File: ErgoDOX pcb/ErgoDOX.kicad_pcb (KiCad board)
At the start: 2 copper layers, 182.8 x 158.9 mm, 77 parts, among them J1 USB, J2 3.5mm, J3 JMP, J4 JMP, SW0:10 SW0:3, SW0:11 SW0:2, SW0:12 SW0:1, SW0:7 SW0:6, SW0:8 SW0:5, SW0:9 SW0:4, SW1:10 SW1:3, SW1:11 SW1:2, SW1:12 SW1:1, SW1:13 SW1:0, SW1:9 SW1:4, SW2:10 SW2:3, SW2:11 SW2:2, SW2:12 SW2:1, SW2:13 SW2:0, SW2:7 SW2:6, SW2:8 SW2:5, SW2:9 SW2:4, SW3:10 SW3:3, SW3:11 SW3:2, SW3:12 SW3:1, SW3:13 SW3:0, SW3:8 SW3:5, SW3:9 SW3:4, SW4:10 SW4:3, SW4:11 SW4:2, SW4:12 SW4:1, SW4:13 SW4:0, SW4:7 SW4:6, SW4:8 SW4:5, SW4:9 SW4:4, SW5:10 SW5:3, SW5:11 SW5:2, SW5:12 SW5:1, SW5:13 SW5:0, SW5:7 SW5:6, SW5:8 SW5:5, SW5:9 SW5:4, U1 TEENSY2.0, U2 MCP23018

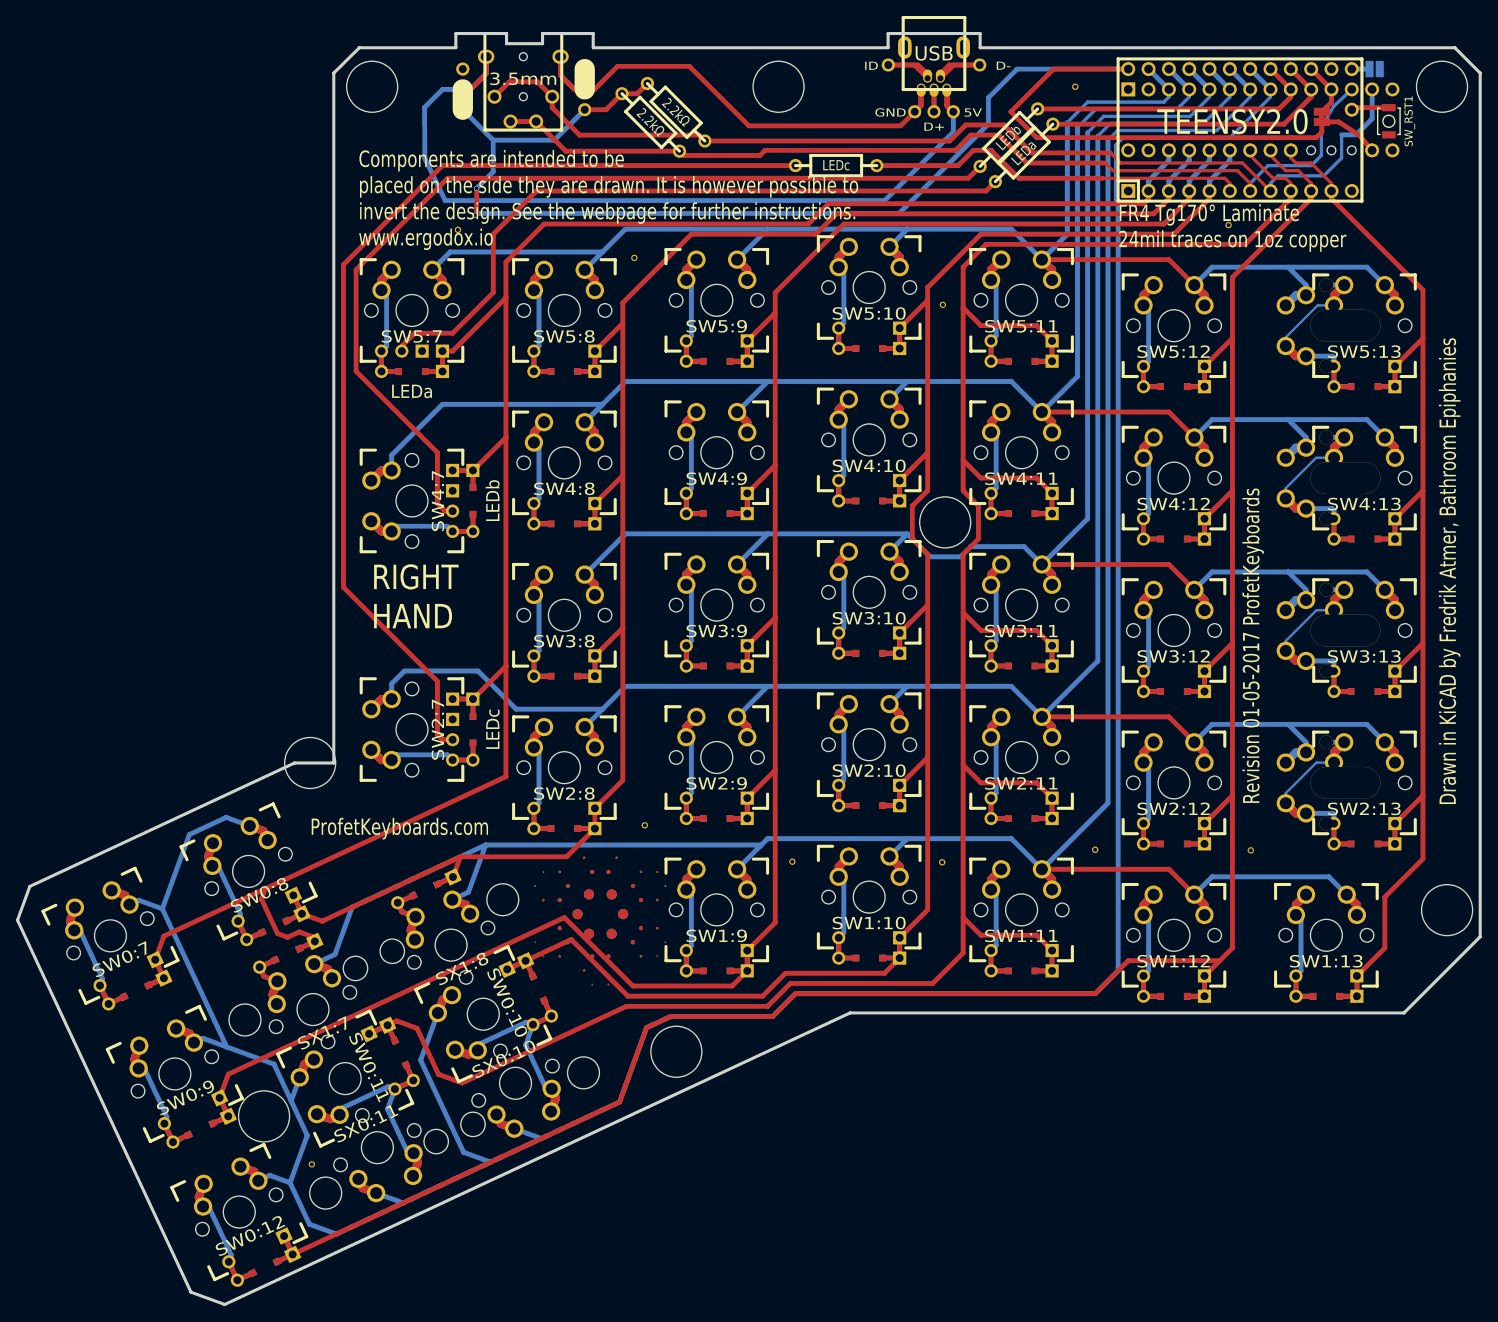
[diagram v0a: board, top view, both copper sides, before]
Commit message: test replace with choc switch
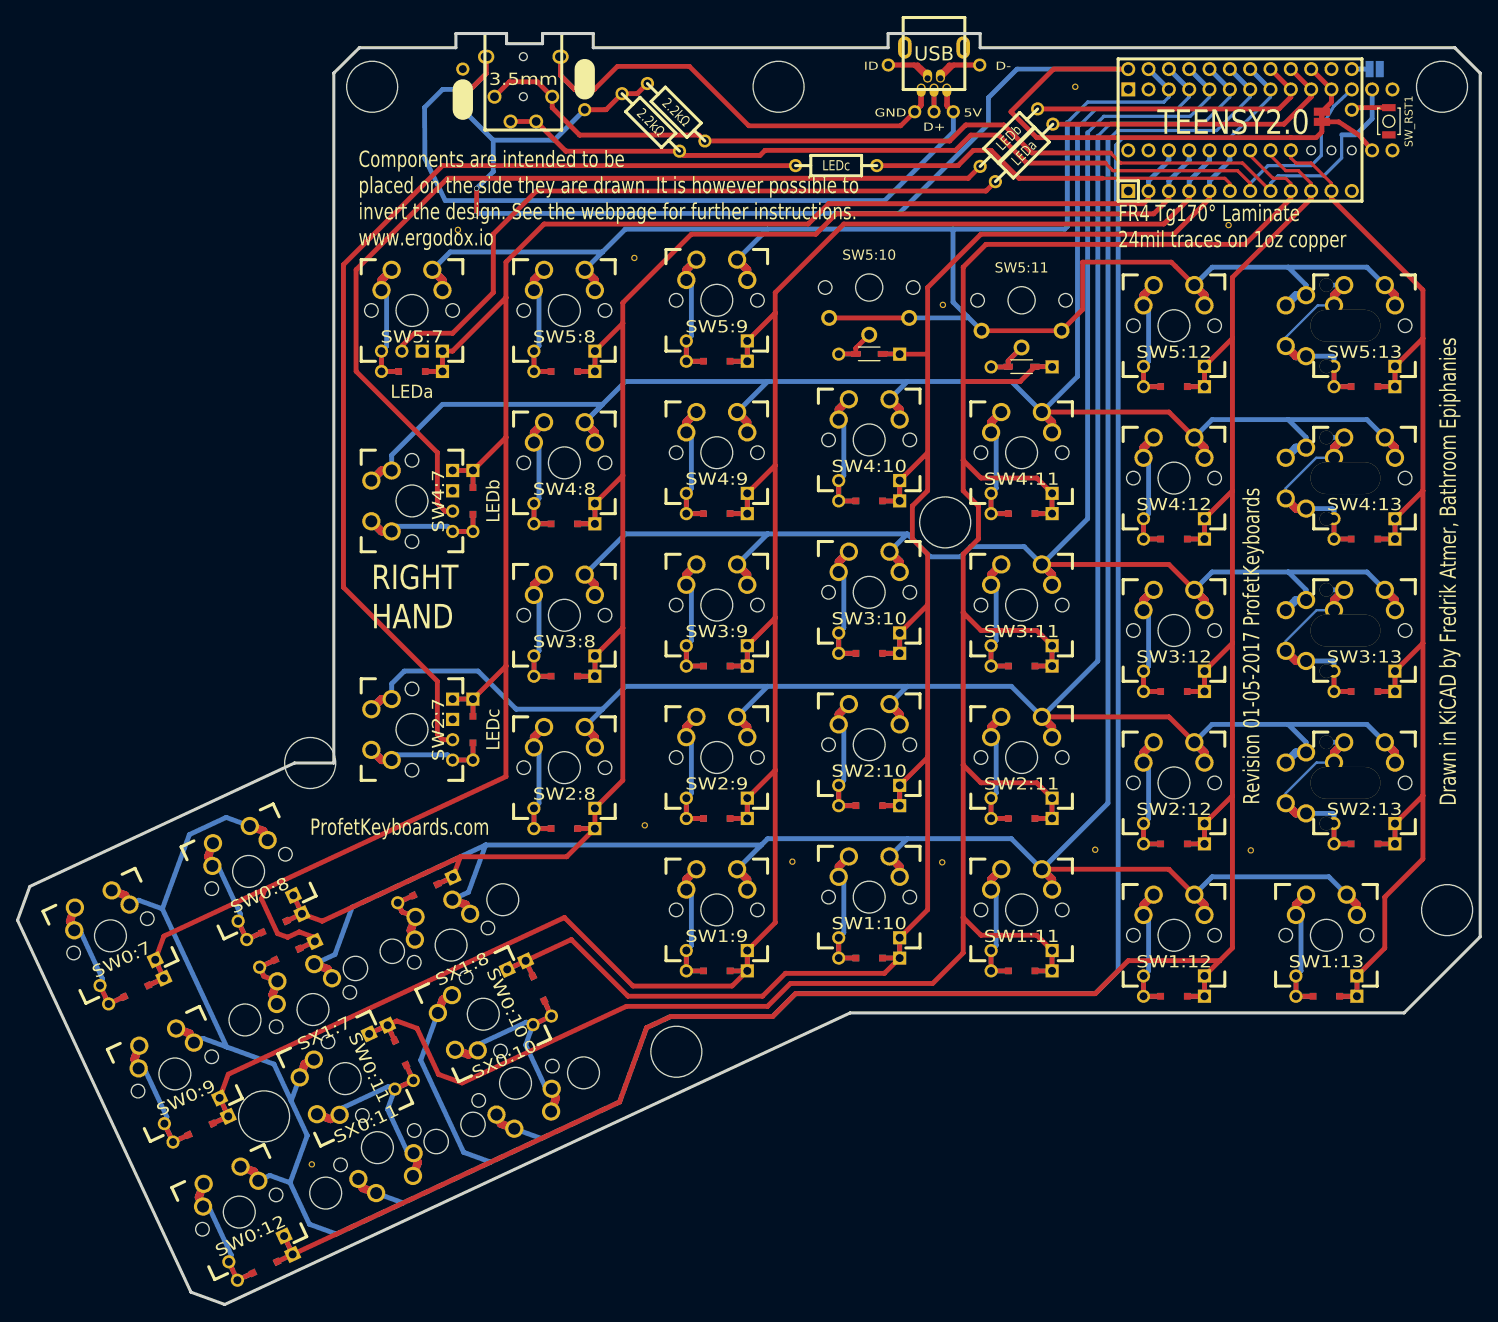
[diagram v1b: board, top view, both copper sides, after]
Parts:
- removed STAR_1: STAR_FRONT, ErgoDOX pcb:STAR
- removed STAR_2: STAR_BACK, ErgoDOX pcb:STAR
- SW5:10, SW5:11: footprint ErgoDOX pcb:MX_FLIP_DIODE -> marbastlib:SW_choc_Reversible_1u
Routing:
- net /ROW5: track 225.1 -> 251.9 mm
- net Net-(SW5:10-Pad2): track 19.4 -> 7.28 mm
- net Net-(SW5:11-Pad2): track 19.4 -> 10.4 mm
- net /COL11: track 316.5 -> 311.9 mm
- net Net-(SW5:13-Pad2): track 38.0 -> 35.1 mm
- net Net-(SW4:13-Pad2): track 38.1 -> 35.2 mm
- net Net-(SW3:13-Pad2): track 38.1 -> 35.2 mm
- net Net-(SW2:13-Pad2): track 37.7 -> 35.2 mm
- net /COL10: track 233.7 -> 231.4 mm
- net /COL1: track 291.8 -> 291.2 mm
- net Net-(J1-Pad5): track 62.3 -> 61.7 mm
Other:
- net class Default removed

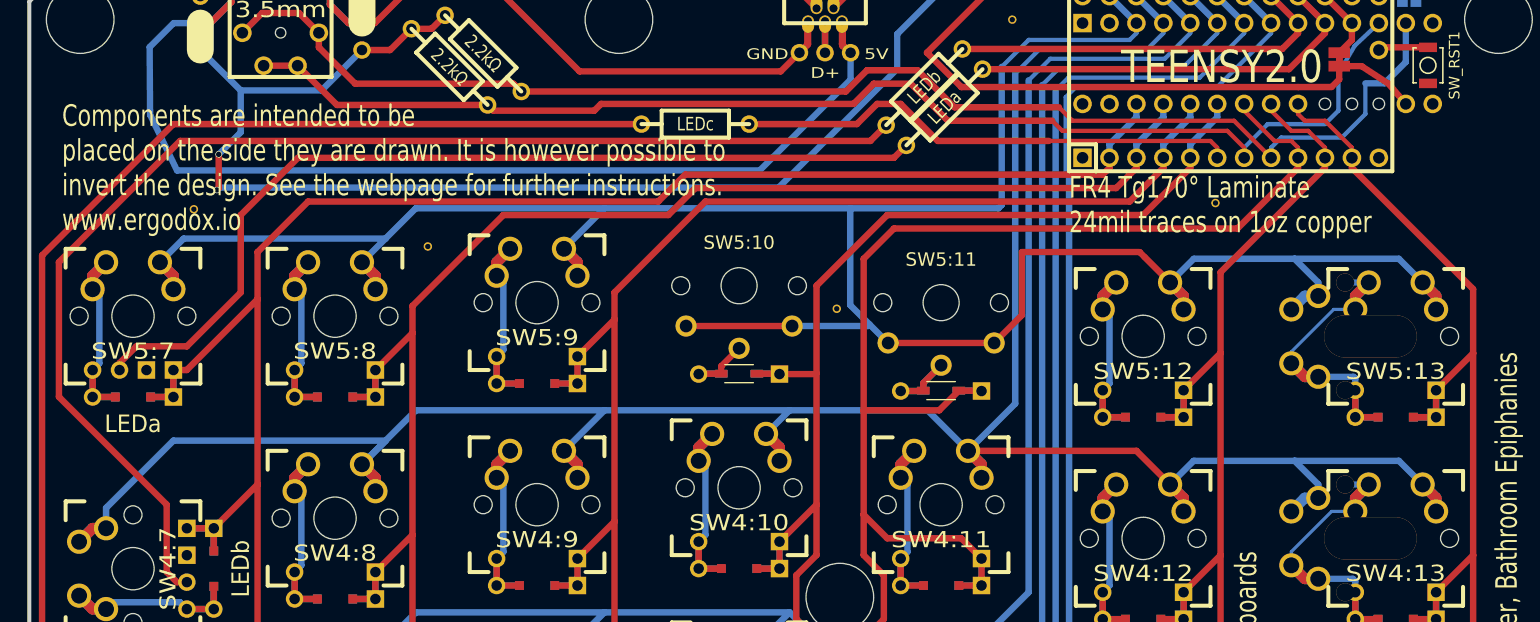
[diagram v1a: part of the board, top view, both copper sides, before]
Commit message: replace first row switches
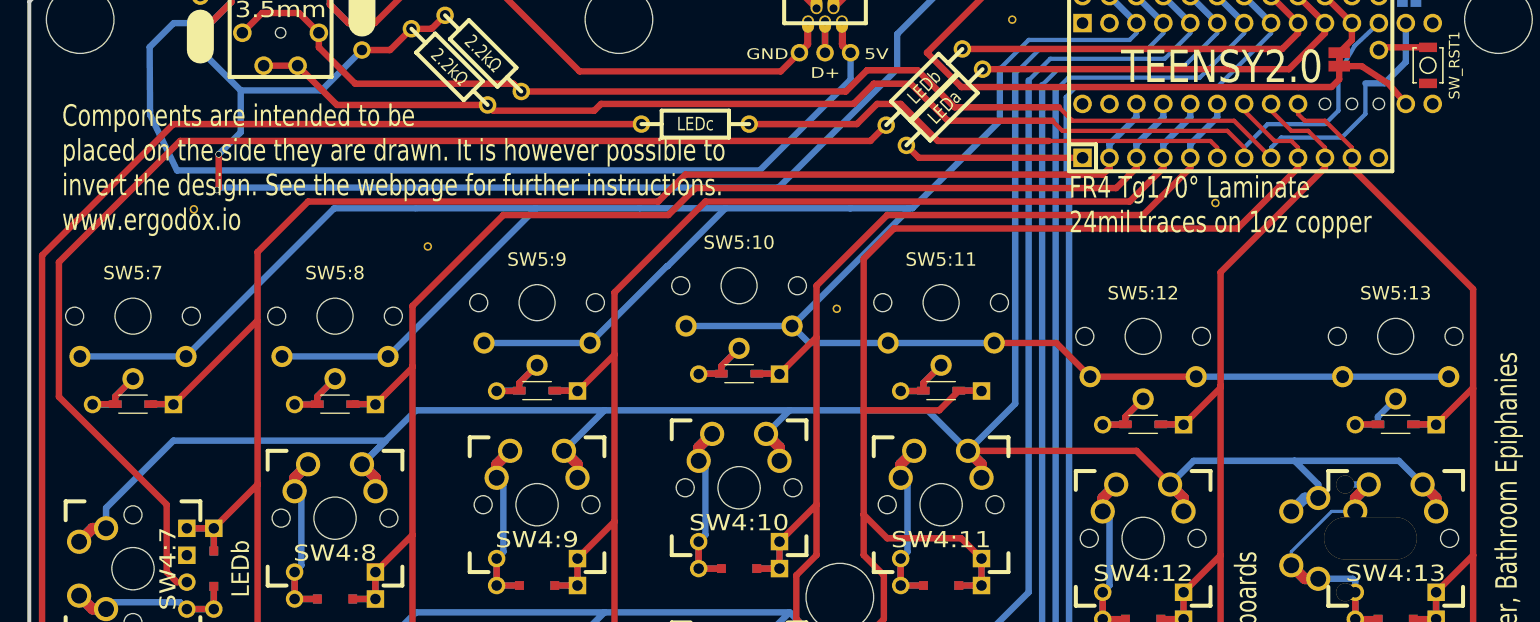
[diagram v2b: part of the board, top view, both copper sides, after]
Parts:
- removed LED_A1: LEDa, MX_LED
- SW5:12, SW5:7, SW5:8, SW5:9: footprint ErgoDOX pcb:MX_FLIP_DIODE -> ErgoDOX pcb:SW_choc_Reversible_1u
- SW5:13: footprint ErgoDOX pcb:MX_FLIP_XX -> ErgoDOX pcb:SW_choc_Reversible_1u
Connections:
- RA1 pad 2: Net-(LED_A1-Pad1) -> GND
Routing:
- net Net-(LED_A1-Pad1): track 87.6 -> 0.00 mm
- net Net-(SW5:13-Pad2): track 35.1 -> 7.28 mm
- net GND: track 2.22 -> 19.3 mm
- net /ROW5: track 251.9 -> 266.7 mm
- net Net-(SW5:8-Pad2): track 19.4 -> 10.4 mm
- net Net-(SW5:12-Pad2): track 19.4 -> 10.4 mm
- net Net-(SW5:7-Pad2): track 19.4 -> 10.4 mm
- net Net-(SW5:9-Pad2): track 19.4 -> 10.4 mm
- net Net-(SW5:10-Pad2): track 7.28 -> 10.4 mm
- net /COL10: track 231.4 -> 232.8 mm
- net /COL4: track 274.3 -> 273.4 mm
- net /COL0: track 159.7 -> 158.8 mm
- net /COL5: track 225.8 -> 225.0 mm
- net /COL1: track 291.2 -> 290.5 mm
